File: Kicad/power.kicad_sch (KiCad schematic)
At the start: 32 parts, among them J7 22112042

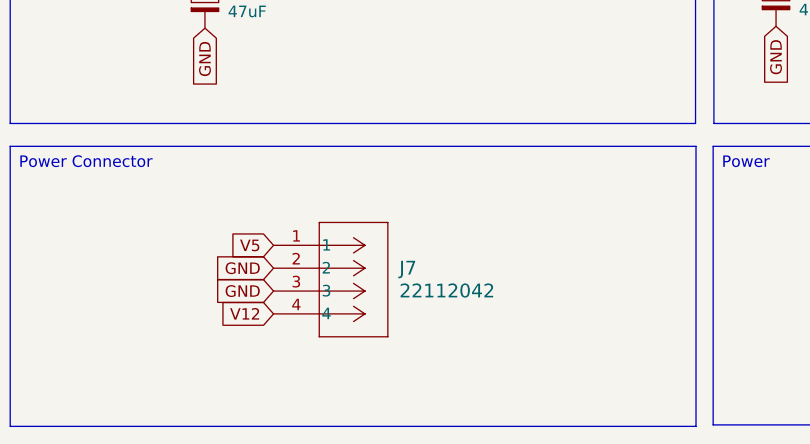
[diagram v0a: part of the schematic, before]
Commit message: Add two missing bulk power caps from old schematics
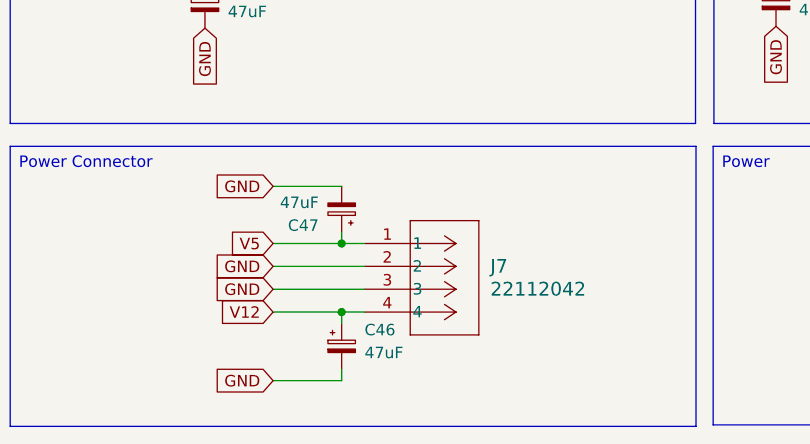
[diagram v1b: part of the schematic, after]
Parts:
- added C46, C47: 47uF, Capacitor_SMD:CP_Elec_6.3x7.7, symbol Device:C_Polarized_Small
- C33, C43, C44, C45: MPN (none) -> KEMET/A765EB476M1ELAE040
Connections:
- net +5V: now also C47.1
- net GND: now also C46.2, C47.2
- net V12: now also C46.1
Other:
- moved on the sheet: J7

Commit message: Add more LCSC parts and mark some parts DNP
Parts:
- C201, C202, C203, C204: LCSC Part # (none) -> C14663
- C33, C43, C44, C45, C46, C47: LCSC Part # (none) -> C41410187
- F1: LCSC Part # (none) -> C434714

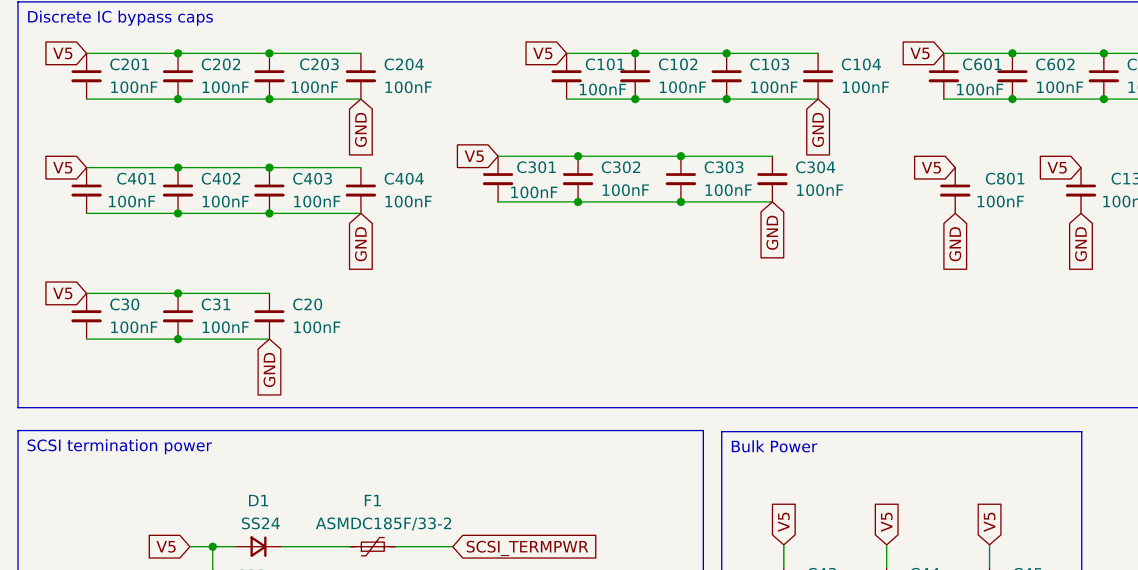
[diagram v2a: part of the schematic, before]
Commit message: Add remaining part numbers, remove C20, C30, C31
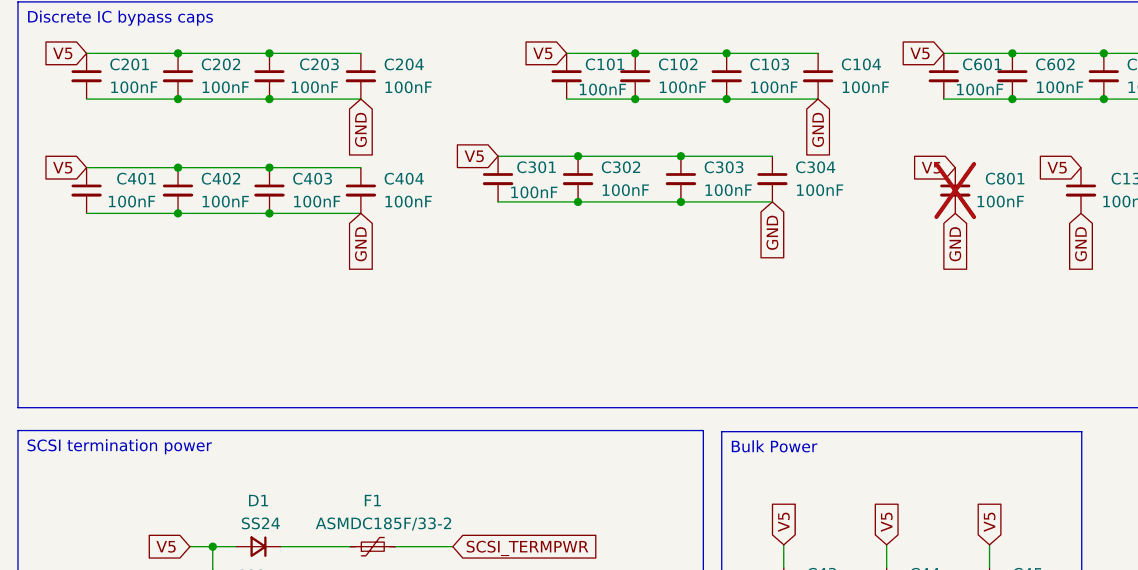
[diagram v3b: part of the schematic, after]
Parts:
- removed C20, C30, C31: 100nF, Capacitor_SMD:C_0603_1608Metric_Pad1.08x0.95mm_HandSolder, symbol Device:C_Small
- C101, C102, C103, C104, C1301, C301, C302, C303, C304, C401, C402, C403, C404: LCSC Part # (none) -> C14663
- C801: LCSC Part # (none) -> C14663; now not fitted
- D1: LCSC Part # (none) -> C43381

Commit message: Fix LCSC parts issues
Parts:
- C33, C43, C44, C45, C46, C47: LCSC Part # C41410187 -> C176321
- C601, C602, C603, C604: LCSC Part # (none) -> C14663
- F1: LCSC Part # C434714 -> C3761950
- J7: LCSC Part # (none) -> C114123
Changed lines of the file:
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@@
 			)
 		)
-		(property "LCSC Part #" ""
+		(property "LCSC Part #" "C14663"
 			(at 152.4 29.21 0)
 			(effects
@@
 			)
 		)
-		(property "LCSC Part #" ""
+		(property "LCSC Part #" "C14663"
 			(at 142.24 29.21 0)
 			(effects
@@
 			)
 		)
-		(property "LCSC Part #" "C434714"
+		(property "LCSC Part #" "C3761950"
 			(at 61.0106 81.4843 90)
 			(effects
@@
 			)
 		)
-		(property "LCSC Part #" "C41410187"
+		(property "LCSC Part #" "C176321"
 			(at 106.68 86.36 0)
 			(effects
@@
 			)
 		)
-		(property "LCSC Part #" "C41410187"
+		(property "LCSC Part #" "C176321"
 			(at 58.42 124.46 0)
 			(effects
@@
 			)
 		)
-		(property "LCSC Part #" "C41410187"
+		(property "LCSC Part #" "C176321"
 			(at 118.11 86.36 0)
 			(effects
@@
 			)
 		)
-		(property "LCSC Part #" "C41410187"
+		(property "LCSC Part #" "C176321"
 			(at 58.42 109.22 0)
 			(effects
@@
 			)
 		)
-		(property "LCSC Part #" ""
+		(property "LCSC Part #" "C14663"
 			(at 124.46 29.21 0)
 			(effects
@@
 			)
 		)
-		(property "LCSC Part #" ""
+		(property "LCSC Part #" "C114123"
 			(at 60.96 113.03 0)
 			(effects
@@
 			)
 		)
+		(property "LCSC Part #" "C14663"
+			(at 132.08 29.21 0)
+			(effects
+				(font
+					(size 1.27 1.27)
+				)
+				(hide yes)
+			)
+		)
 		(pin "1"
 		)
@@
 			)
 		)
-		(property "LCSC Part #" "C41410187"
+		(property "LCSC Part #" "C176321"
 			(at 129.54 86.36 0)
 			(effects
@@
 			)
 		)
-		(property "LCSC Part #" "C41410187"
+		(property "LCSC Part #" "C176321"
 			(at 43.2306 86.5643 0)
 			(effects

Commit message: Use APAQ Tech 250AVHA470M0606 not AVEA
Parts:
- C33, C43, C44, C45, C46, C47: LCSC Part # C176321 -> C369909
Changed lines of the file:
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@@
 			)
 		)
-		(property "LCSC Part #" "C176321"
+		(property "LCSC Part #" "C369909"
 			(at 106.68 86.36 0)
 			(effects
@@
 			)
 		)
-		(property "LCSC Part #" "C176321"
+		(property "LCSC Part #" "C369909"
 			(at 58.42 124.46 0)
 			(effects
@@
 			)
 		)
-		(property "LCSC Part #" "C176321"
+		(property "LCSC Part #" "C369909"
 			(at 118.11 86.36 0)
 			(effects
@@
 			)
 		)
-		(property "LCSC Part #" "C176321"
+		(property "LCSC Part #" "C369909"
 			(at 58.42 109.22 0)
 			(effects
@@
 			)
 		)
-		(property "LCSC Part #" "C176321"
+		(property "LCSC Part #" "C369909"
 			(at 129.54 86.36 0)
 			(effects
@@
 			)
 		)
-		(property "LCSC Part #" "C176321"
+		(property "LCSC Part #" "C369909"
 			(at 43.2306 86.5643 0)
 			(effects

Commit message: Clean up schematics
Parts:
- F1: LCSC Part # C3761950 -> C135379
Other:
- moved on the sheet: C101, C102, C103, C104, C1301, C201, C202, C203, C204, C301, C302, C303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

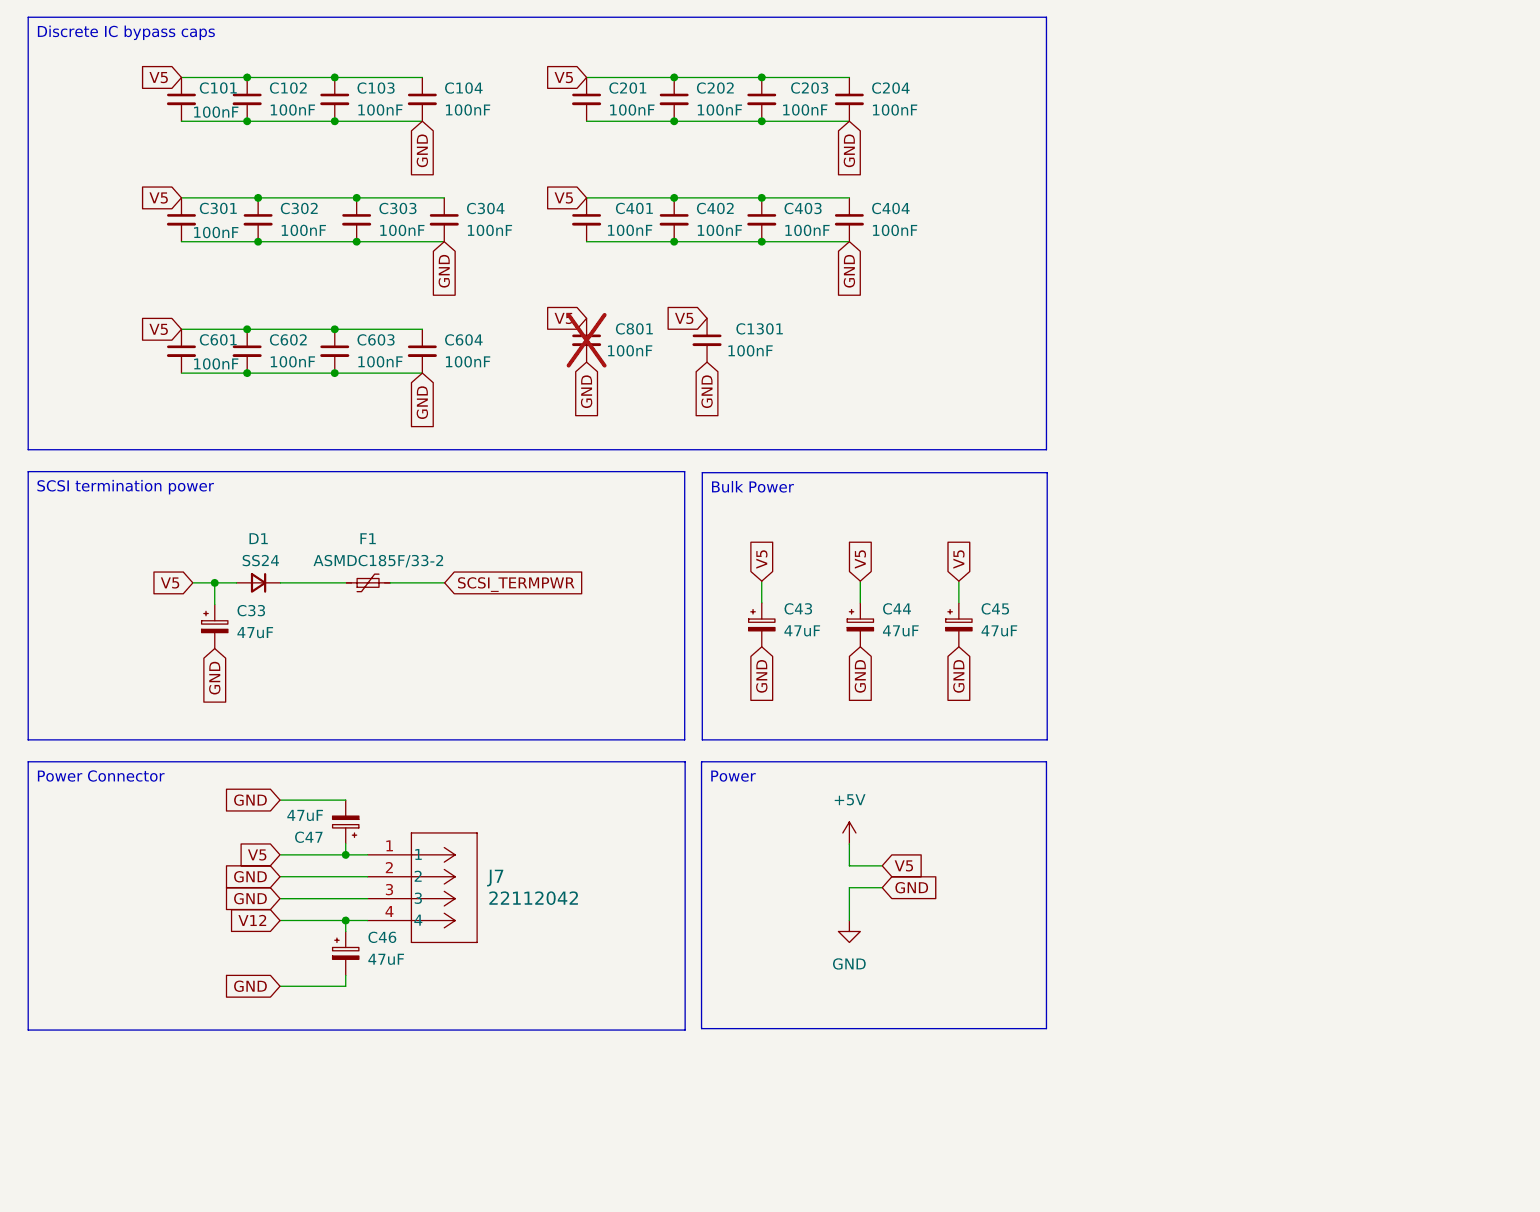
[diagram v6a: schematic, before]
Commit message: Add fiducials and clean up schematics
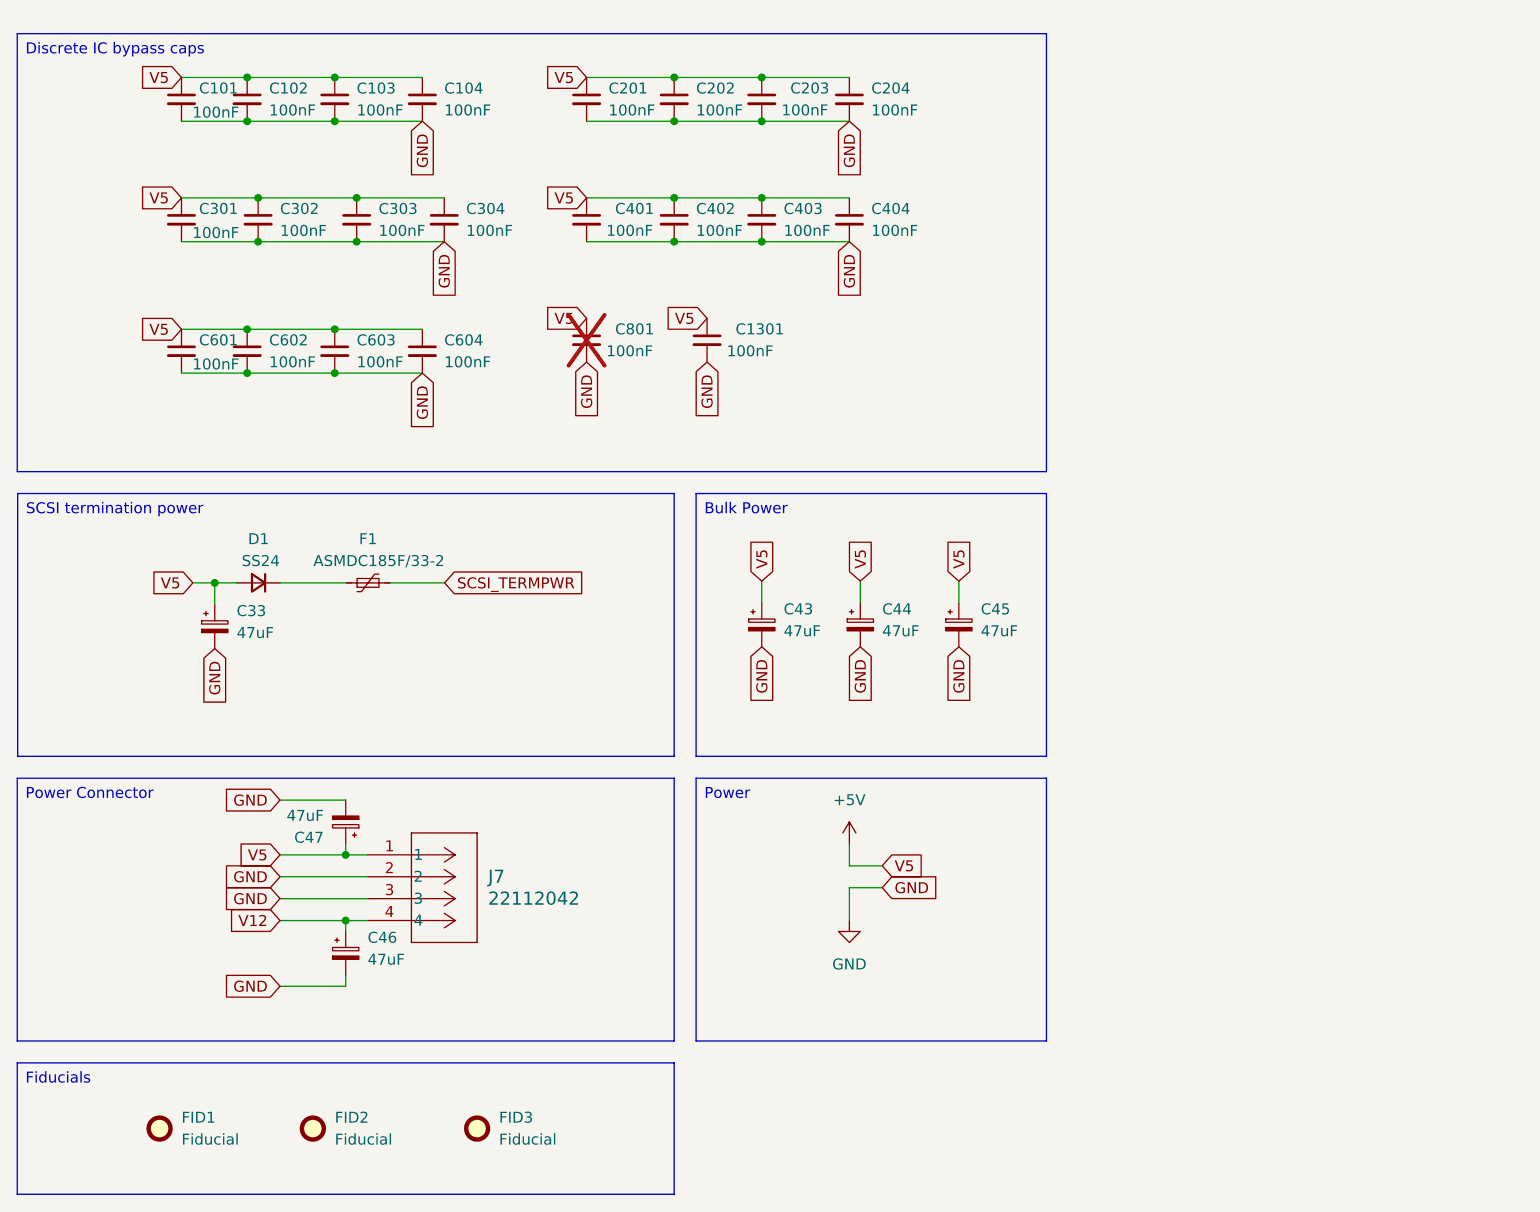
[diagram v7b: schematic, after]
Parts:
- added FID1, FID2, FID3: Fiducial, kicad-official/Fiducial.pretty:Fiducial_0.5mm_Mask1.5mm, symbol Mechanical:Fiducial
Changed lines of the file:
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@@
 	(text_box "SCSI termination power\n"
 		(exclude_from_sim no)
-		(at 21.59 73.66 0)
-		(size 76.1494 31.115)
+		(at 20.3706 76.2 0)
+		(size 76.1494 30.48)
 		(margins 0.9525 0.9525 0.9525 0.9525)
 		(stroke
@@
 	(text_box "Power Connector\n"
 		(exclude_from_sim no)
-		(at 21.59 107.315 0)
-		(size 76.2 31.115)
+		(at 20.32 109.22 0)
+		(size 76.2 30.48)
 		(margins 0.9525 0.9525 0.9525 0.9525)
 		(stroke
@@
 		)
 	)
+	(text_box "Fiducials"
+		(exclude_from_sim no)
+		(at 20.32 142.24 0)
+		(size 76.2 15.2399)
+		(margins 0.9525 0.9525 0.9525 0.9525)
+		(stroke
+			(width 0)
+			(type solid)
+		)
+		(fill
+			(type none)
+		)
+		(effects
+			(font
+				(size 1.27 1.27)
+			)
+			(justify left top)
+		)
+	)
 	(text_box "Discrete IC bypass caps\n"
 		(exclude_from_sim no)
-		(at 21.59 20.955 0)
-		(size 118.11 50.165)
+		(at 20.32 22.86 0)
+		(size 119.38 50.8)
 		(margins 0.9525 0.9525 0.9525 0.9525)
 		(stroke
@@
 	(text_box "Bulk Power\n"
 		(exclude_from_sim no)
-		(at 99.7818 73.7824 0)
-		(size 40.005 30.9926)
+		(at 99.06 76.2 0)
+		(size 40.64 30.48)
 		(margins 0.9525 0.9525 0.9525 0.9525)
 		(stroke
@@
 	(text_box "Power\n"
 		(exclude_from_sim no)
-		(at 99.695 107.315 0)
-		(size 40.005 30.9505)
+		(at 99.06 109.22 0)
+		(size 40.64 30.4799)
 		(margins 0.9525 0.9525 0.9525 0.9525)
 		(stroke
@@
 	)
 	(symbol
+		(lib_id "Mechanical:Fiducial")
+		(at 73.66 149.86 0)
+		(unit 1)
+		(exclude_from_sim no)
+		(in_bom no)
+		(on_board yes)
+		(dnp no)
+		(fields_autoplaced yes)
+		(property "Reference" "FID3"
+			(at 76.2 148.5899 0)
+			(effects
+				(font
+					(size 1.27 1.27)
+				)
+				(justify left)
+			)
+		)
+		(property "Value" "Fiducial"
+			(at 76.2 151.1299 0)
+			(effects
+				(font
+					(size 1.27 1.27)
+				)
+				(justify left)
+			)
+		)
+		(property "Footprint" "kicad-official/Fiducial.pretty:Fiducial_0.5mm_Mask1.5mm"
+			(at 73.66 149.86 0)
+			(effects
+				(font
+					(size 1.27 1.27)
+				)
+				(hide yes)
+			)
+		)
+		(property "Datasheet" "~"
+			(at 73.66 149.86 0)
+			(effects
+				(font
+					(size 1.27 1.27)
+				)
+				(hide yes)
+			)
+		)
+		(property "Description" "Fiducial Marker"
+			(at 73.66 149.86 0)
+			(effects
+				(font
+					(size 1.27 1.27)
+				)
+				(hide yes)
+			)
+		)
+		(instances
+			(project ""
+				(path "/8f9f4021-47aa-41d9-bea7-f6ccf72098bb/166c366c-e5f9-4398-87d9-75fc4b57be99"
+					(reference "FID3")
+					(unit 1)
+				)
+			)
+		)
+	)
+	(symbol
+		(lib_id "Mechanical:Fiducial")
+		(at 54.61 149.86 0)
+		(unit 1)
+		(exclude_from_sim no)
+		(in_bom no)
+		(on_board yes)
+		(dnp no)
+		(fields_autoplaced yes)
+		(property "Reference" "FID2"
+			(at 57.15 148.5899 0)
+			(effects
+				(font
+					(size 1.27 1.27)
+				)
+				(justify left)
+			)
+		)
+		(property "Value" "Fiducial"
+			(at 57.15 151.1299 0)
+			(effects
+				(font
+					(size 1.27 1.27)
+				)
+				(justify left)
+			)
+		)
+		(property "Footprint" "kicad-official/Fiducial.pretty:Fiducial_0.5mm_Mask1.5mm"
+			(at 54.61 149.86 0)
+			(effects
+				(font
+					(size 1.27 1.27)
+				)
+				(hide yes)
+			)
+		)
+		(property "Datasheet" "~"
+			(at 54.61 149.86 0)
+			(effects
+				(font
+					(size 1.27 1.27)
+				)
+				(hide yes)
+			)
+		)
+		(property "Description" "Fiducial Marker"
+			(at 54.61 149.86 0)
+			(effects
+				(font
+					(size 1.27 1.27)
+				)
+				(hide yes)
+			)
+		)
+		(instances
+			(project ""
+				(path "/8f9f4021-47aa-41d9-bea7-f6ccf72098bb/166c366c-e5f9-4398-87d9-75fc4b57be99"
+					(reference "FID2")
+					(unit 1)
+				)
+			)
+		)
+	)
+	(symbol
 		(lib_id "power:GND")
 		(at 116.84 125.73 0)
@@
 					(unit 1)
 				)
+			)
+		)
+	)
+	(symbol
+		(lib_id "Mechanical:Fiducial")
+		(at 36.83 149.86 0)
+		(unit 1)
+		(exclude_from_sim no)
+		(in_bom no)
+		(on_board yes)
+		(dnp no)
+		(fields_autoplaced yes)
+		(property "Reference" "FID1"
+			(at 39.37 148.5899 0)
+			(effects
+				(font
+					(size 1.27 1.27)
+				)
+				(justify left)
+			)
+		)
+		(property "Value" "Fiducial"
+			(at 39.37 151.1299 0)
+			(effects
+				(font
+					(size 1.27 1.27)
+				)
+				(justify left)
+			)
+		)
+		(property "Footprint" "kicad-official/Fiducial.pretty:Fiducial_0.5mm_Mask1.5mm"
+			(at 36.83 149.86 0)
+			(effects
+				(font
+					(size 1.27 1.27)
+				)
+				(hide yes)
+			)
+		)
+		(property "Datasheet" "~"
+			(at 36.83 149.86 0)
+			(effects
+				(font
+					(size 1.27 1.27)
+				)
+				(hide yes)
+			)
+		)
+		(property "Description" "Fiducial Marker"
+			(at 36.83 149.86 0)
+			(effects
+				(font
+					(size 1.27 1.27)
+				)
+				(hide yes)
+			)
+		)
+		(instances
+			(project ""
+				(path "/8f9f4021-47aa-41d9-bea7-f6ccf72098bb/166c366c-e5f9-4398-87d9-75fc4b57be99"
+					(reference "FID1")
+					(unit 1)
+				)
